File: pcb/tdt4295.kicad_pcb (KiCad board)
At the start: 6 copper layers, 119.8 x 96.8 mm, 157 parts, among them J1 FPGA_DEBUG, J2 DE15_Socket_HighDensity, J4 Conn_ST_STDC14, J5 Micro_SD_Card, J6 Conn_02x05_Odd_Even, J7 USB_C_Receptacle_USB2.0_14P, J8 USB_C_Receptacle_USB2.0_14P, SW1 SW_BLUE, SW2 SW_BLACK, SW3 SW_Push, U1 XC7A50T-FTG256, U2 S70KL1283DPBHV020, U3 W25Q128JVS, U4 TPS54325PWP.d, U5 TPS54294PWP, U6 STM32U595ZJTx, U7 TPS2051CDBV, U8 USBLC6-2SC6, Y1 ASE-20MHz, Y2 16MHz

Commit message: fpga button
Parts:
- moved SW3 1.14 mm to (90.8, 89.4)
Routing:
- net GND: track 472.1 -> 482.9 mm, vias 124 -> 122
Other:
- board text removed: "RESET"
- board text removed: "USER_BUTTON"

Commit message: pcb: add logo and names
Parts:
- added G***: LOGO, LOGO, F.Cu at (158.2, 66.5)
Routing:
- net /fpga/USER_BUTTON: track 30.5 -> 60.6 mm, vias 2 -> 4
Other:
- board text added: "Adrian Christoffer Håheim Hoff Mats Kvanvik Mikal Samland-Johansen Øyvind Nestvold Sivert Underdal Vegard Kyrkjedelen Hovland Fredrik Robertsen"
- board text added: "RESET"
- board text added: "USER_BUTTON"

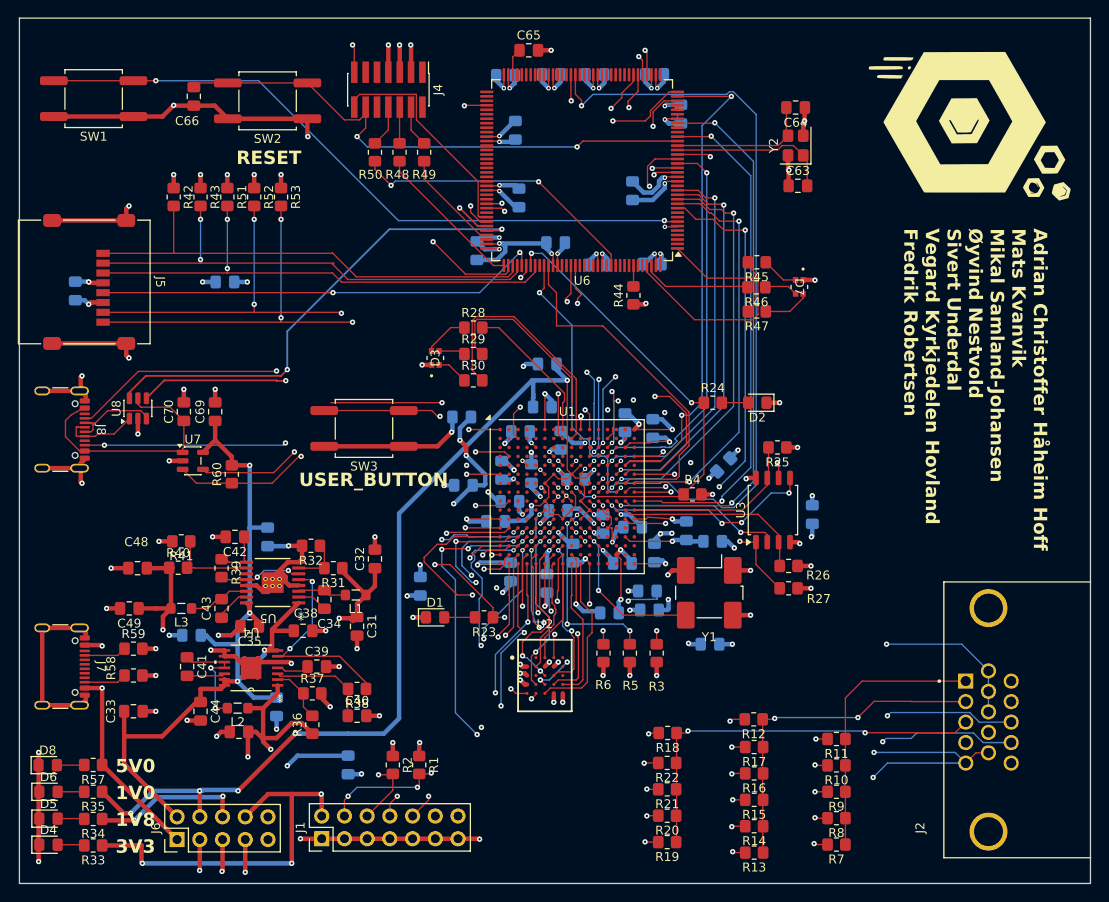
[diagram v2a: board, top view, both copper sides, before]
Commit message: pcb: fix drc
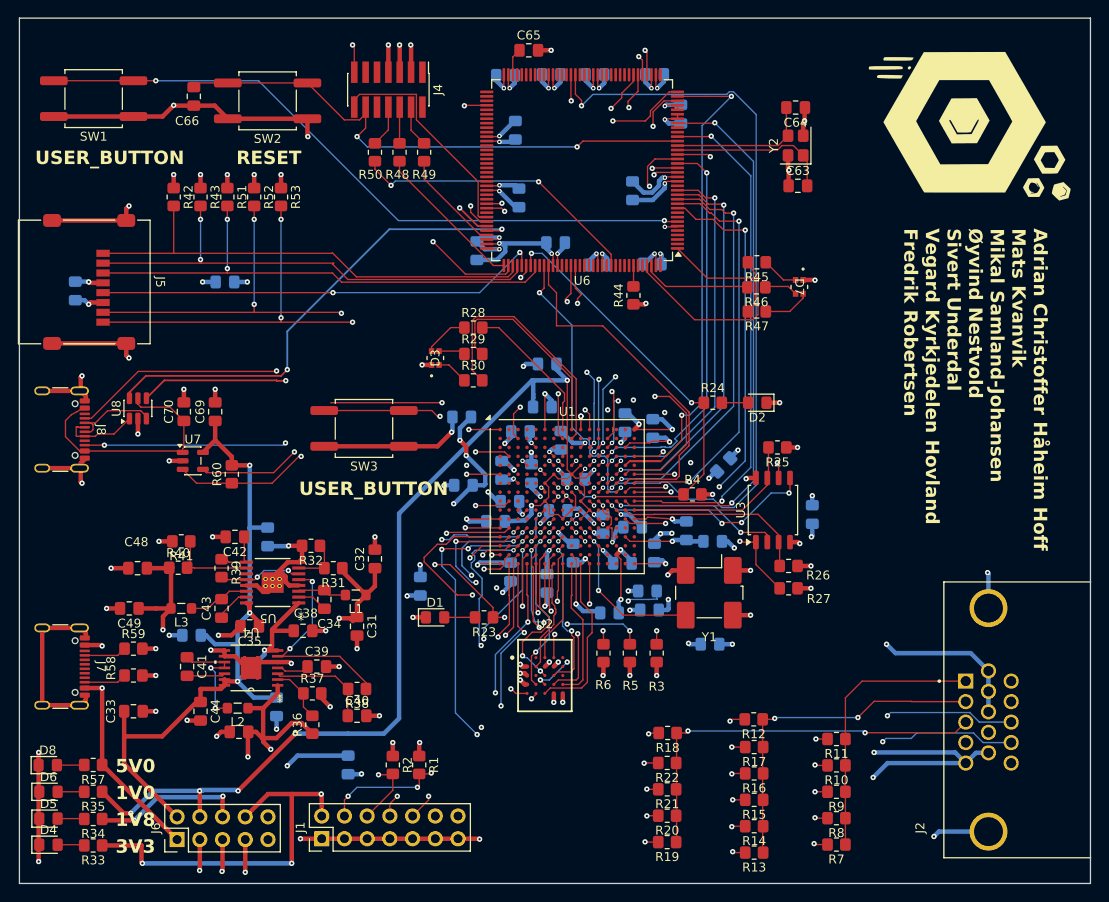
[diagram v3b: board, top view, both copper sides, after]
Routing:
- net GND: track 482.9 -> 493.2 mm, vias 122 -> 124
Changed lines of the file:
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@@
 		(layer "Edge.Cuts")
 	)
+	(gr_text "USER_BUTTON"
+		(at 54 60 0)
+		(layer "F.SilkS")
+		(effects
+			(font
+				(size 1.5 1.5)
+				(thickness 0.3)
+				(bold yes)
+			)
+			(justify left bottom)
+		)
+	)
 	(gr_text "5V0"
 		(at 63 128 0)
@@
 	)
 	(gr_text "USER_BUTTON"
-		(at 83.5 96 0)
+		(at 83.5 97 0)
 		(layer "F.SilkS")
 		(effects
@@
 	)
 	(segment
-		(start 160.5975 125.645)
-		(end 159.2025 125.645)
-		(width 0.15)
-		(layer "F.Cu")
-		(net "GND")
-	)
-	(segment
 		(start 120.9 75.5)
 		(end 122.2 75.5)
@@
 	)
 	(segment
-		(start 159.2025 125.645)
-		(end 158.0575 126.79)
-		(width 0.15)
-		(layer "F.Cu")
-		(net "GND")
-	)
-	(segment
 		(start 100.57 89.8)
 		(end 98.995 91.375)
@@
 	)
 	(via
+		(at 160.5 105.5)
+		(size 0.6)
+		(drill 0.25)
+		(layers "F.Cu" "B.Cu")
+		(net "GND")
+	)
+	(via
 		(at 117.5 92)
 		(size 0.5)
@@
 	)
 	(via
+		(at 154.5 135)
+		(size 0.6)
+		(drill 0.25)
+		(layers "F.Cu" "B.Cu")
+		(net "GND")
+	)
+	(via
 		(at 123.262497 69.8375)
 		(size 0.5)
@@
 	)
 	(segment
+		(start 155.045 134.455)
+		(end 154.5 135)
+		(width 0.5)
+		(layer "B.Cu")
+		(net "GND")
+	)
+	(segment
 		(start 105.631739 70.5375)
 		(end 106.5625 69.606739)
@@
 	)
 	(segment
+		(start 160.5975 125.645)
+		(end 159.2025 125.645)
+		(width 0.5)
+		(layer "B.Cu")
+		(net "GND")
+	)
+	(segment
 		(start 111.755 86.255)
 		(end 111 85.5)
@@
 		(start 160.5975 118.775)
 		(end 160.5975 121.065)
-		(width 0.15)
+		(width 0.5)
 		(layer "B.Cu")
 		(net "GND")
@@
 		(start 160.5975 116.485)
 		(end 160.5975 118.775)
-		(width 0.15)
+		(width 0.5)
 		(layer "B.Cu")
 		(net "GND")
@@
 	)
 	(segment
+		(start 160.5975 116.485)
+		(end 158.6125 114.5)
+		(width 0.5)
+		(layer "B.Cu")
+		(net "GND")
+	)
+	(segment
 		(start 128.685 102)
 		(end 126.97 102)
@@
 		(start 149.31 126.79)
 		(end 147.7 128.4)
-		(width 0.15)
+		(width 0.5)
 		(layer "B.Cu")
 		(net "GND")
@@
 	)
 	(segment
-		(start 157.6125 113.5)
-		(end 160.5975 116.485)
-		(width 0.15)
+		(start 160.5975 105.5975)
+		(end 160.5 105.5)
+		(width 0.5)
 		(layer "B.Cu")
 		(net "GND")
@@
 	)
 	(segment
+		(start 159.2025 125.645)
+		(end 158.0575 126.79)
+		(width 0.5)
+		(layer "B.Cu")
+		(net "GND")
+	)
+	(segment
+		(start 160.5975 109.465)
+		(end 160.5975 105.5975)
+		(width 0.5)
+		(layer "B.Cu")
+		(net "GND")
+	)
+	(segment
 		(start 70.4625 112.5)
 		(end 69 112.5)
@@
 		(start 158.0575 126.79)
 		(end 149.31 126.79)
-		(width 0.15)
+		(width 0.5)
 		(layer "B.Cu")
 		(net "GND")
@@
 	)
 	(segment
+		(start 150.2 114.5)
+		(end 149.2 113.5)
+		(width 0.5)
+		(layer "B.Cu")
+		(net "GND")
+	)
+	(segment
 		(start 104.455 99.77)
 		(end 102.52 99.77)
@@
 	)
 	(segment
+		(start 158.6125 114.5)
+		(end 150.2 114.5)
+		(width 0.5)
+		(layer "B.Cu")
+		(net "GND")
+	)
+	(segment
 		(start 115.8625 70.737497)
 		(end 116.762497 69.8375)
@@
 		(start 156.8675 125.6)
 		(end 158.0575 126.79)
-		(width 0.15)
-		(layer "B.Cu")
-		(net "GND")
-	)
-	(segment
-		(start 149.2 113.5)
-		(end 157.6125 113.5)
-		(width 0.15)
+		(width 0.5)
 		(layer "B.Cu")
 		(net "GND")
@@
 	)
 	(segment
+		(start 160.5975 134.455)
+		(end 155.045 134.455)
+		(width 0.5)
+		(layer "B.Cu")
+		(net "GND")
+	)
+	(segment
 		(start 108.86 82.17)
 		(end 108.6 82.43)
@@
 		(start 147.8 125.6)
 		(end 156.8675 125.6)
-		(width 0.15)
+		(width 0.5)
 		(layer "B.Cu")
 		(net "GND")
@@
 	)
 	(segment
-		(start 113.5 111.25)
-		(end 113.5 100)
-		(width 0.15)
-		(layer "B.Cu")
-		(net "Net-(U1C-INIT_B_0)")
-	)
-	(segment
 		(start 114.6 99.05)
 		(end 114.5 99.2)
@@
 		(net "Net-(U1C-INIT_B_0)")
 	)
+	(segment
+		(start 113.5 111.25)
+		(end 113.5 100)
+		(width 0.15)
+		(layer "In4.Cu")
+		(net "Net-(U1C-INIT_B_0)")
+	)

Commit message: pcb: clear all DRCs
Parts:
- moved R53 2.00 mm to (83.5, 63.5)
- moved R52 1.50 mm to (80.0, 63.5)
- moved D4 1.00 mm to (55.5, 136.9)
- moved R33 1.00 mm to (60.5, 137.0)
- moved R51 1.00 mm to (76.5, 63.5)
- moved D8 0.50 mm to (55.4, 126.5)
- moved R43 0.50 mm to (73.0, 63.5)
- moved R57 0.50 mm to (60.5, 126.5)
- moved D5 0.46 mm to (55.5, 133.5)
- moved R34 0.46 mm to (60.5, 133.5)
- moved C68 0.36 mm to (58.9, 74.0)
- moved J5 0.36 mm to (59.9, 73.0)
- moved SW2 0.25 mm to (80.0, 52.5)
- moved J2 0.19 mm to (160.4, 122.0)
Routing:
- net /fpga/USER_BUTTON: track 60.6 -> 32.0 mm, vias 4 -> 2
- net +1V8: track 120.3 -> 123.7 mm
- net GND: track 493.2 -> 494.8 mm
- net /MCU/SD_DAT1: track 65.2 -> 66.0 mm
- net +3V3: track 228.6 -> 227.9 mm

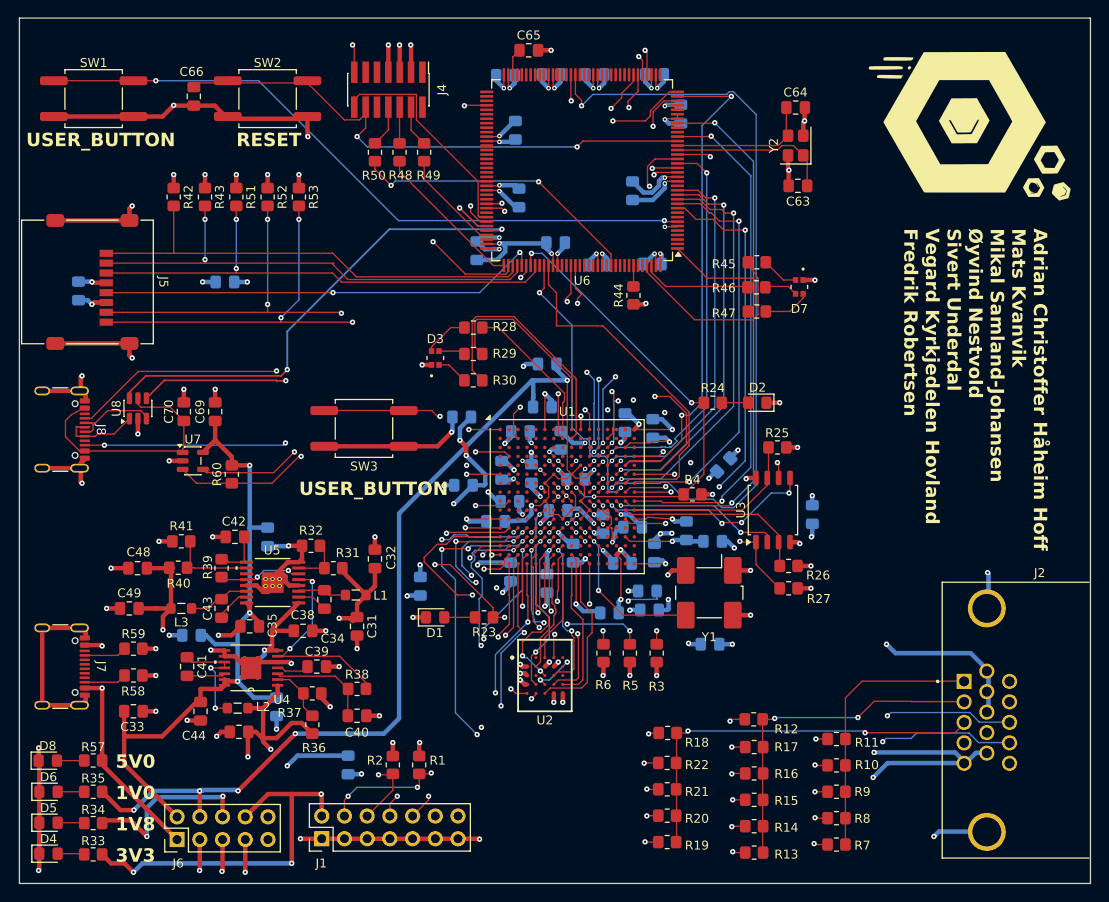
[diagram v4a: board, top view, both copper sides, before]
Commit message: usb-c diff pair + 3d models + redundant wire deletion
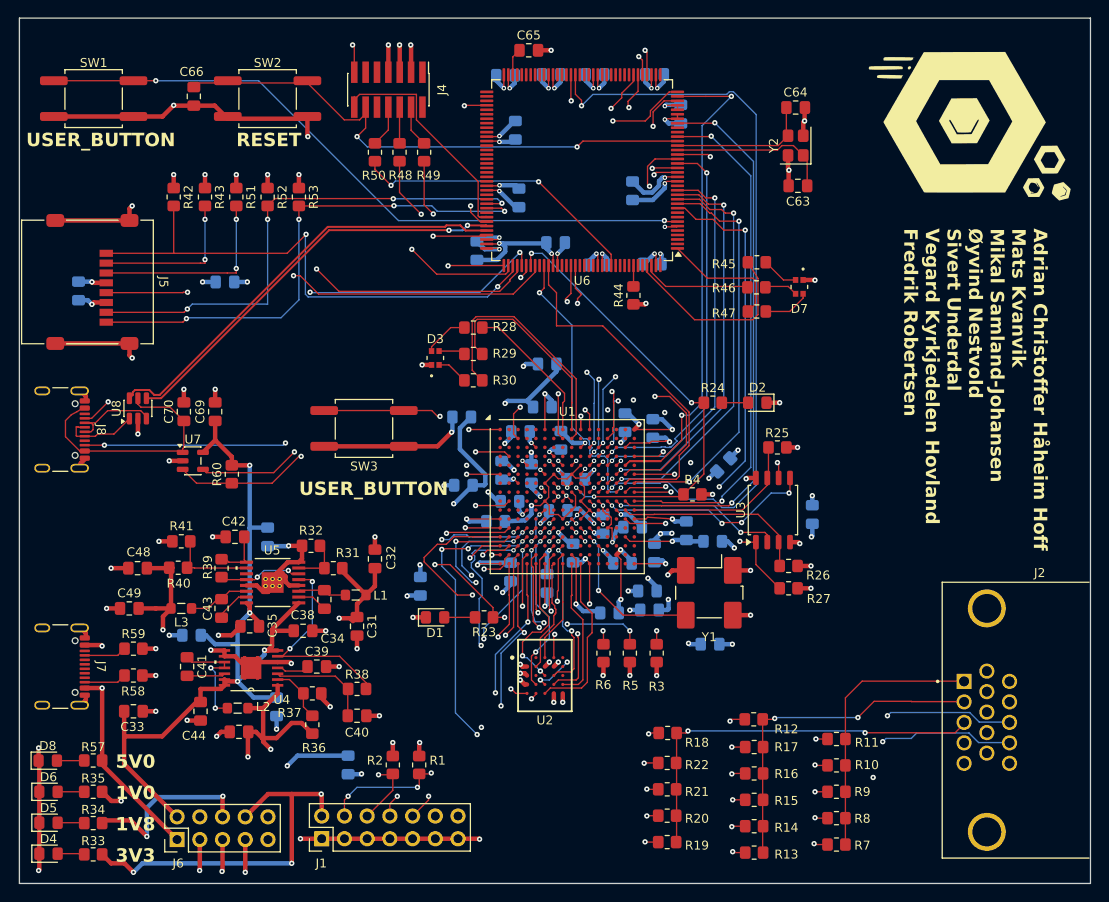
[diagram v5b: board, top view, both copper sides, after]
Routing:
- net GND: track 494.8 -> 413.6 mm, vias 124 -> 118
- net +1V0: track 224.2 -> 160.8 mm, vias 11 -> 8
- net /MCU/SD_DAT2: track 53.2 -> 61.5 mm, vias 0 -> 2
- net /MCU/SD_DAT1: track 66.0 -> 58.5 mm
- net /MCU/SD_DAT0: track 63.4 -> 57.9 mm
- net USB_FS_P: track 54.1 -> 48.8 mm, vias 2 -> 0
- net /MCU/MCU_STLINK_JTMS: track 11.6 -> 15.6 mm, vias 0 -> 2
- net +1V8: track 123.7 -> 119.9 mm, vias 9 -> 7
- net USB_FS_N: track 49.6 -> 46.1 mm
- net /MCU/MCU_STLINK_JCLK: track 17.2 -> 20.2 mm, vias 0 -> 2
- net /MCU/SD_CMD: track 57.4 -> 58.7 mm, vias 2 -> 3
- net /MCU/SD_DAT3: track 54.8 -> 55.9 mm, vias 2 -> 3
- net /MCU/SD_CLK: track 50.0 -> 49.7 mm, vias 2 -> 3

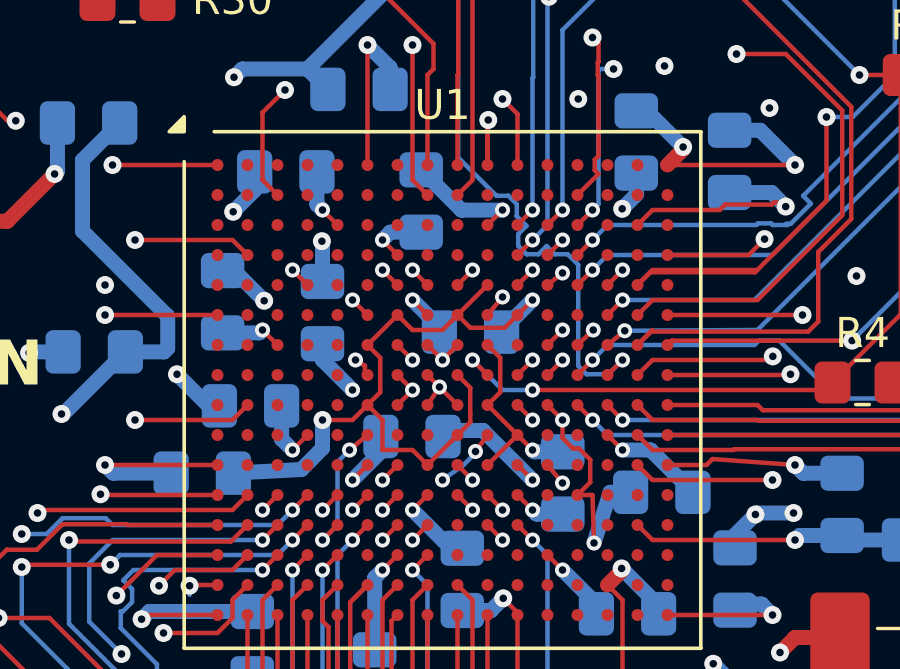
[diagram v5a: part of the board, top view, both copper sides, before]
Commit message: pcb/fpga: fix power supply
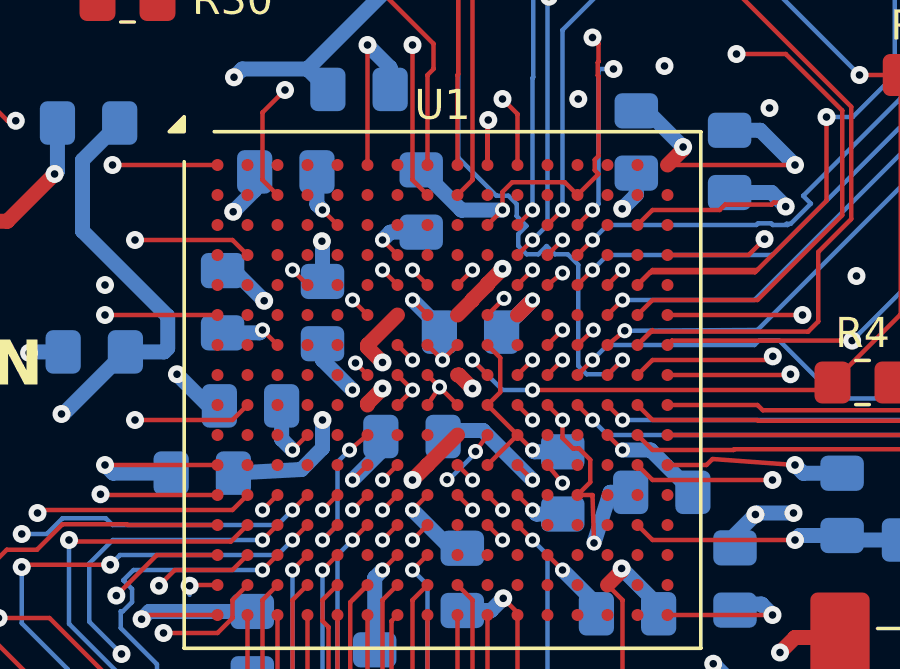
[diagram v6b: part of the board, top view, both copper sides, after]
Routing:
- net +3V3: track 227.9 -> 237.5 mm
- net +1V0: track 160.8 -> 166.4 mm, vias 8 -> 13
- net /fpga/TDO_0: track 53.1 -> 54.2 mm
